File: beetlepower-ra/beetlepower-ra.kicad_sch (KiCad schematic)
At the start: 14 parts, among them J1 Battery, J2 OUT2, J3 OUT3, J4 OUT4, J5 Conn_01x03_Male, U1 MC7805

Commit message: Beetlepower right angle board
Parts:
- C1: value C -> 2.2uf; footprint beetlepower-xt30:C-pth-and-smd -> Capacitor_SMD:C_0805_2012Metric_Pad1.18x1.45mm_HandSolder
- R1: value R -> 1.5k; footprint beetlepower-xt30:Resistor-pth-and-smd -> Resistor_SMD:R_0805_2012Metric_Pad1.20x1.40mm_HandSolder
- U1: LCSC (none) -> C54285
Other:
- note added: "Assuming we use a white or blue LED, VF= 3.0 a 4S pack at apprx 16V, we need to drop 13V across a resistor and have 10mA so 1.5k is good."
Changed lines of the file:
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@@
     (stroke (width 0) (type solid) (color 0 0 0 0))
+  )
+  (text "Assuming we use a white or blue LED,\nVF= 3.0\n\na 4S pack at apprx 16V,\n\nwe need to drop 13V across a resistor and have 10mA\nso 1.5k is good."
+    (at 129.54 55.88 0)
+    (effects (font (size 1.27 1.27)) (justify left bottom))
   )
   (label "B+IN" (at 78.105 71.755 180)
@@
       (effects (font (size 1.27 1.27)) (justify left))
     )
-    (property "Value" "R" (id 1) (at 139.7 83.8199 0)
-      (effects (font (size 1.27 1.27)) (justify left))
-    )
-    (property "Footprint" "beetlepower-xt30:Resistor-pth-and-smd" (id 2) (at 135.382 81.915 90)
+    (property "Value" "1.5k" (id 1) (at 139.7 83.8199 0)
+      (effects (font (size 1.27 1.27)) (justify left))
+    )
+    (property "Footprint" "Resistor_SMD:R_0805_2012Metric_Pad1.20x1.40mm_HandSolder" (id 2) (at 135.382 81.915 90)
       (effects (font (size 1.27 1.27)) hide)
     )
@@
       (effects (font (size 1.27 1.27)) (justify left))
     )
-    (property "Value" "C" (id 1) (at 190.5 78.7399 0)
-      (effects (font (size 1.27 1.27)) (justify left))
-    )
-    (property "Footprint" "beetlepower-xt30:C-pth-and-smd" (id 2) (at 187.6552 80.645 0)
+    (property "Value" "2.2uf" (id 1) (at 190.5 78.7399 0)
+      (effects (font (size 1.27 1.27)) (justify left))
+    )
+    (property "Footprint" "Capacitor_SMD:C_0805_2012Metric_Pad1.18x1.45mm_HandSolder" (id 2) (at 187.6552 80.645 0)
       (effects (font (size 1.27 1.27)) hide)
     )
@@
       (effects (font (size 1.27 1.27)) hide)
     )
+    (property "LCSC" "C54285" (id 4) (at 173.99 70.485 0)
+      (effects (font (size 1.27 1.27)) hide)
+    )
     (pin "1")
     (pin "2")
@@
     )
     (path "/e185f8e6-3657-4e72-8333-bee9105cbce1"
-      (reference "C1") (unit 1) (value "C") (footprint "beetlepower-xt30:C-pth-and-smd")
+      (reference "C1") (unit 1) (value "2.2uf") (footprint "Capacitor_SMD:C_0805_2012Metric_Pad1.18x1.45mm_HandSolder")
     )
     (path "/bb80ddbd-1c56-4016-90b2-e3035e5a6227"
@@
     )
     (path "/41ea4b02-622d-4689-9b91-59bb0aaceccc"
-      (reference "R1") (unit 1) (value "R") (footprint "beetlepower-xt30:Resistor-pth-and-smd")
+      (reference "R1") (unit 1) (value "1.5k") (footprint "Resistor_SMD:R_0805_2012Metric_Pad1.20x1.40mm_HandSolder")
     )
     (path "/c3c1864a-2ff6-40d5-b620-ea0426ce4ee0"

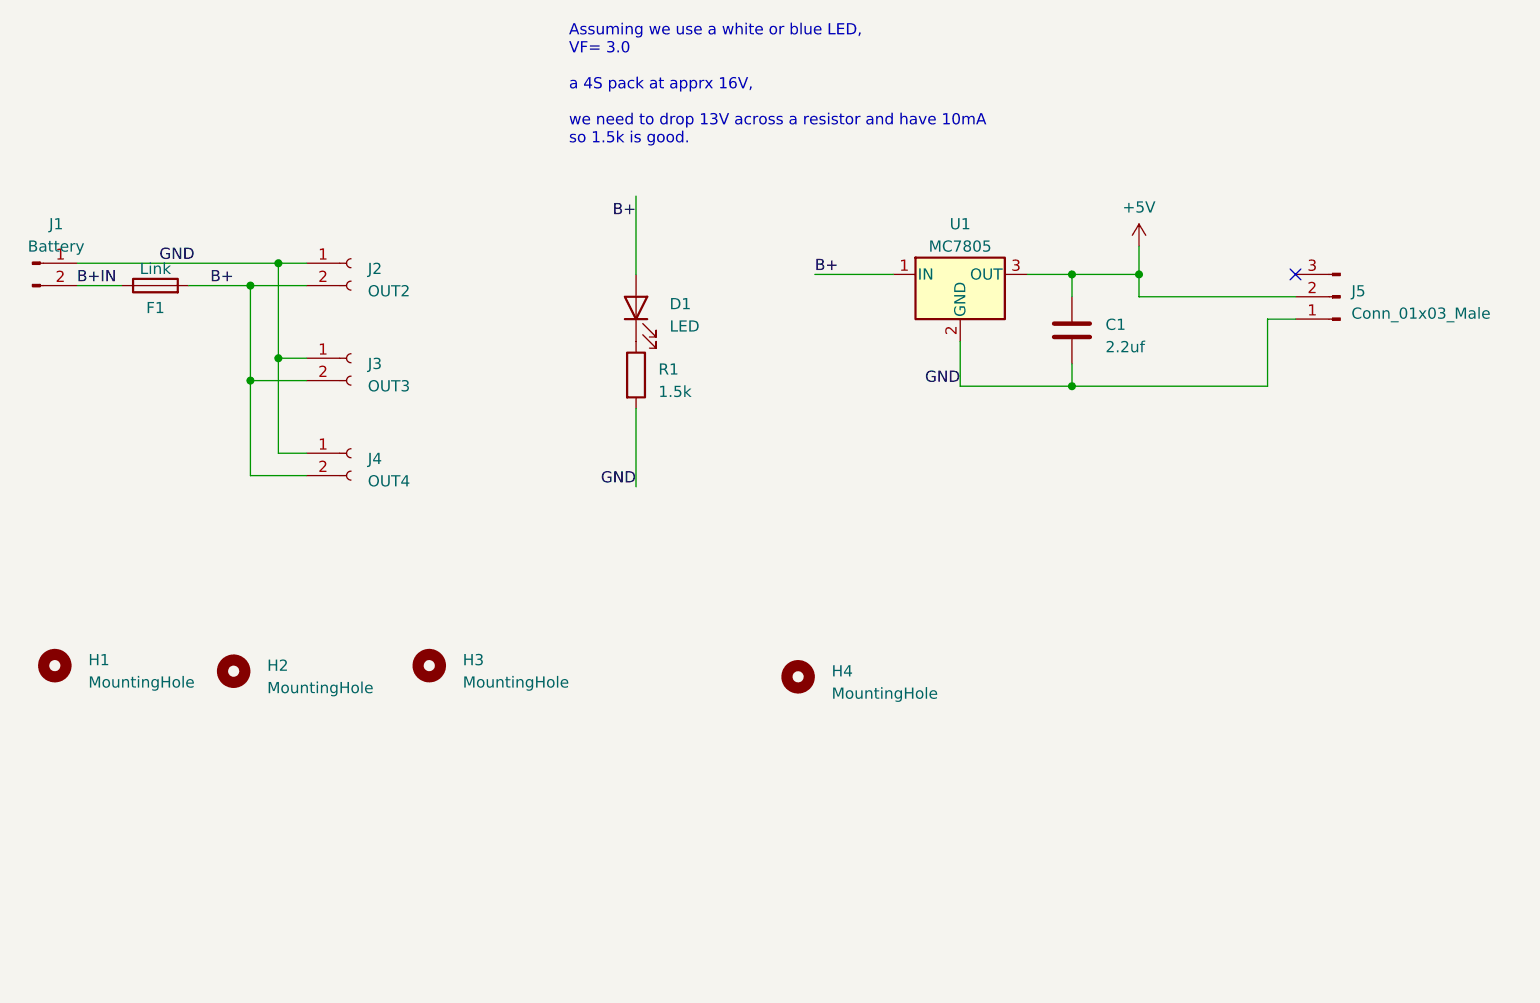
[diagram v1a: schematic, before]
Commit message: Another version of Beetlepower RA with cable tie slots
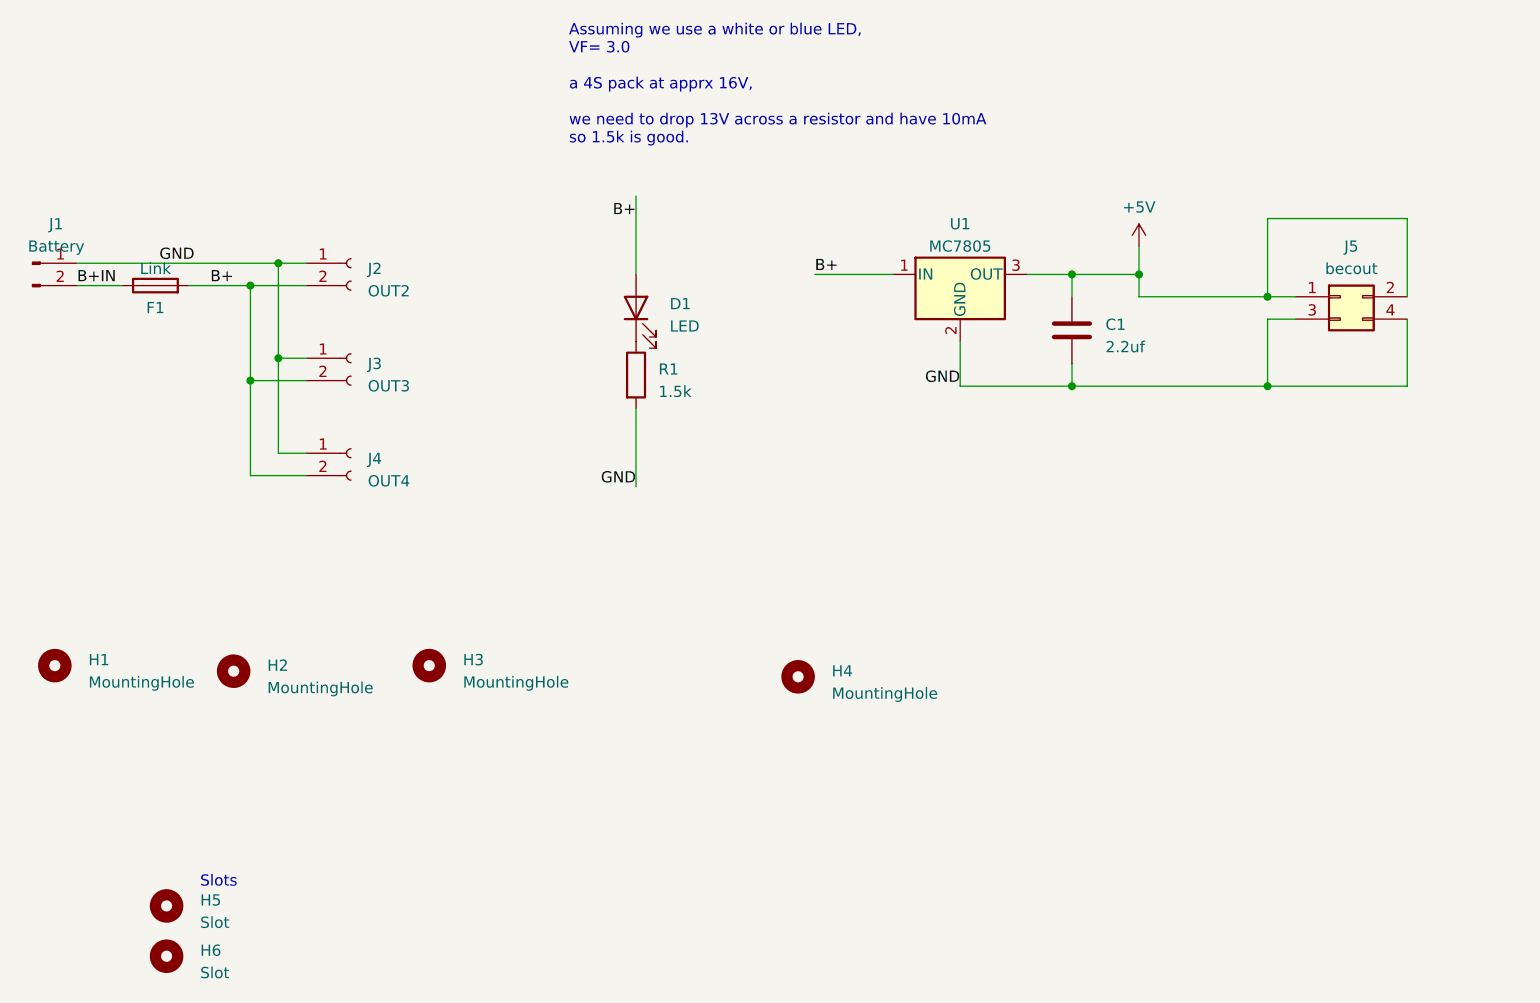
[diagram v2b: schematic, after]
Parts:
- removed J5: Conn_01x03_Male, Connector_PinHeader_2.54mm:PinHeader_1x03_P2.54mm_Vertical, symbol Connector:Conn_01x03_Male
- added H5, H6: Slot, beetlepower-xt30:cabletie_slot, symbol Mechanical:MountingHole
- added J5: becout, Connector_PinHeader_2.54mm:PinHeader_2x02_P2.54mm_Vertical, symbol Connector_Generic:Conn_02x02_Odd_Even
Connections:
- net +5V: now also J5.1 (Pin_1), J5.2 (Pin_2)
- net GND: now also J5.3 (Pin_3), J5.4 (Pin_4)
- no-connect marks 1 -> 0
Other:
- note added: "Slots"
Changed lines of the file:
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@@
   (junction (at 186.69 83.185) (diameter 0.9144) (color 0 0 0 0))
   (junction (at 194.31 70.485) (diameter 0.9144) (color 0 0 0 0))
-  (no_connect (at 212.09 70.485))
+  (junction (at 208.915 73.025) (diameter 0.9144) (color 0 0 0 0))
+  (junction (at 208.915 83.185) (diameter 0.9144) (color 0 0 0 0))
   (wire (pts (xy 73.66 69.215) (xy 96.52 69.215))
     (stroke (width 0) (type solid) (color 0 0 0 0))
@@
     (stroke (width 0) (type solid) (color 0 0 0 0))
   )
+  (wire (pts (xy 208.915 64.135) (xy 208.915 73.025))
+    (stroke (width 0) (type solid) (color 0 0 0 0))
+  )
+  (wire (pts (xy 208.915 73.025) (xy 194.31 73.025))
+    (stroke (width 0) (type solid) (color 0 0 0 0))
+  )
   (wire (pts (xy 208.915 75.565) (xy 212.09 75.565))
     (stroke (width 0) (type solid) (color 0 0 0 0))
@@
     (stroke (width 0) (type solid) (color 0 0 0 0))
   )
-  (wire (pts (xy 212.09 73.025) (xy 194.31 73.025))
-    (stroke (width 0) (type solid) (color 0 0 0 0))
+  (wire (pts (xy 212.09 73.025) (xy 208.915 73.025))
+    (stroke (width 0) (type solid) (color 0 0 0 0))
+  )
+  (wire (pts (xy 224.79 64.135) (xy 208.915 64.135))
+    (stroke (width 0) (type solid) (color 0 0 0 0))
+  )
+  (wire (pts (xy 224.79 73.025) (xy 224.79 64.135))
+    (stroke (width 0) (type solid) (color 0 0 0 0))
+  )
+  (wire (pts (xy 224.79 75.565) (xy 224.79 83.185))
+    (stroke (width 0) (type solid) (color 0 0 0 0))
+  )
+  (wire (pts (xy 224.79 83.185) (xy 208.915 83.185))
+    (stroke (width 0) (type solid) (color 0 0 0 0))
+  )
+  (text "Slots" (at 87.63 140.335 0)
+    (effects (font (size 1.27 1.27)) (justify left bottom))
   )
   (text "Assuming we use a white or blue LED,\nVF= 3.0\n\na 4S pack at apprx 16V,\n\nwe need to drop 13V across a resistor and have 10mA\nso 1.5k is good."
@@
     )
     (property "Datasheet" "~" (id 3) (at 71.12 114.935 0)
+      (effects (font (size 1.27 1.27)) hide)
+    )
+  )
+  (symbol (lib_id "Mechanical:MountingHole") (at 83.82 142.24 0) (unit 1)
+    (in_bom yes) (on_board yes) (fields_autoplaced)
+    (property "Reference" "H5" (id 0) (at 87.63 141.6049 0)
+      (effects (font (size 1.27 1.27)) (justify left))
+    )
+    (property "Value" "Slot" (id 1) (at 87.63 144.1449 0)
+      (effects (font (size 1.27 1.27)) (justify left))
+    )
+    (property "Footprint" "beetlepower-xt30:cabletie_slot" (id 2) (at 83.82 142.24 0)
+      (effects (font (size 1.27 1.27)) hide)
+    )
+    (property "Datasheet" "~" (id 3) (at 83.82 142.24 0)
+      (effects (font (size 1.27 1.27)) hide)
+    )
+  )
+  (symbol (lib_id "Mechanical:MountingHole") (at 83.82 147.955 0) (unit 1)
+    (in_bom yes) (on_board yes) (fields_autoplaced)
+    (property "Reference" "H6" (id 0) (at 87.63 147.3199 0)
+      (effects (font (size 1.27 1.27)) (justify left))
+    )
+    (property "Value" "Slot" (id 1) (at 87.63 149.8599 0)
+      (effects (font (size 1.27 1.27)) (justify left))
+    )
+    (property "Footprint" "beetlepower-xt30:cabletie_slot" (id 2) (at 83.82 147.955 0)
+      (effects (font (size 1.27 1.27)) hide)
+    )
+    (property "Datasheet" "~" (id 3) (at 83.82 147.955 0)
       (effects (font (size 1.27 1.27)) hide)
     )
@@
     (pin "2")
   )
-  (symbol (lib_id "Connector:Conn_01x03_Male") (at 217.17 73.025 180) (unit 1)
-    (in_bom yes) (on_board yes) (fields_autoplaced)
-    (property "Reference" "J5" (id 0) (at 218.44 72.3899 0)
-      (effects (font (size 1.27 1.27)) (justify right))
-    )
-    (property "Value" "Conn_01x03_Male" (id 1) (at 218.44 74.9299 0)
-      (effects (font (size 1.27 1.27)) (justify right))
-    )
-    (property "Footprint" "Connector_PinHeader_2.54mm:PinHeader_1x03_P2.54mm_Vertical" (id 2) (at 217.17 73.025 0)
+  (symbol (lib_id "Device:C") (at 186.69 76.835 0) (unit 1)
+    (in_bom yes) (on_board yes) (fields_autoplaced)
+    (property "Reference" "C1" (id 0) (at 190.5 76.1999 0)
+      (effects (font (size 1.27 1.27)) (justify left))
+    )
+    (property "Value" "2.2uf" (id 1) (at 190.5 78.7399 0)
+      (effects (font (size 1.27 1.27)) (justify left))
+    )
+    (property "Footprint" "Capacitor_SMD:C_0805_2012Metric_Pad1.18x1.45mm_HandSolder" (id 2) (at 187.6552 80.645 0)
+      (effects (font (size 1.27 1.27)) hide)
+    )
+    (property "Datasheet" "~" (id 3) (at 186.69 76.835 0)
+      (effects (font (size 1.27 1.27)) hide)
+    )
+    (pin "1")
+    (pin "2")
+  )
+  (symbol (lib_id "Connector_Generic:Conn_02x02_Odd_Even") (at 217.17 73.025 0) (unit 1)
+    (in_bom yes) (on_board yes) (fields_autoplaced)
+    (property "Reference" "J5" (id 0) (at 218.44 67.31 0))
+    (property "Value" "becout" (id 1) (at 218.44 69.85 0))
+    (property "Footprint" "Connector_PinHeader_2.54mm:PinHeader_2x02_P2.54mm_Vertical" (id 2) (at 217.17 73.025 0)
       (effects (font (size 1.27 1.27)) hide)
     )
@@
     (pin "2")
     (pin "3")
-  )
-  (symbol (lib_id "Device:C") (at 186.69 76.835 0) (unit 1)
-    (in_bom yes) (on_board yes) (fields_autoplaced)
-    (property "Reference" "C1" (id 0) (at 190.5 76.1999 0)
-      (effects (font (size 1.27 1.27)) (justify left))
-    )
-    (property "Value" "2.2uf" (id 1) (at 190.5 78.7399 0)
-      (effects (font (size 1.27 1.27)) (justify left))
-    )
-    (property "Footprint" "Capacitor_SMD:C_0805_2012Metric_Pad1.18x1.45mm_HandSolder" (id 2) (at 187.6552 80.645 0)
-      (effects (font (size 1.27 1.27)) hide)
-    )
-    (property "Datasheet" "~" (id 3) (at 186.69 76.835 0)
-      (effects (font (size 1.27 1.27)) hide)
-    )
-    (pin "1")
-    (pin "2")
+    (pin "4")
   )
   (symbol (lib_id "Regulator_Linear:L7805") (at 173.99 70.485 0) (unit 1)
@@
       (reference "H4") (unit 1) (value "MountingHole") (footprint "MountingHole:MountingHole_3.2mm_M3")
     )
+    (path "/e6c44bdf-32f0-43ae-a0a2-77912286eaa9"
+      (reference "H5") (unit 1) (value "Slot") (footprint "beetlepower-xt30:cabletie_slot")
+    )
+    (path "/7acfadbe-ba00-4238-972d-1bcfa34ea07d"
+      (reference "H6") (unit 1) (value "Slot") (footprint "beetlepower-xt30:cabletie_slot")
+    )
     (path "/c30f7975-f802-4364-88da-79d2aa62035f"
       (reference "J1") (unit 1) (value "Battery") (footprint "beetlepower-xt30:XT30U-M")
@@
       (reference "J4") (unit 1) (value "OUT4") (footprint "beetlepower-xt30:XT30U-F")
     )
-    (path "/b40c0ce1-c7ff-4265-94ae-366c97ae60c3"
-      (reference "J5") (unit 1) (value "Conn_01x03_Male") (footprint "Connector_PinHeader_2.54mm:PinHeader_1x03_P2.54mm_Vertical")
+    (path "/52142dd9-9f0a-46d1-b2b9-9d9fe863039d"
+      (reference "J5") (unit 1) (value "becout") (footprint "Connector_PinHeader_2.54mm:PinHeader_2x02_P2.54mm_Vertical")
     )
     (path "/41ea4b02-622d-4689-9b91-59bb0aaceccc"
